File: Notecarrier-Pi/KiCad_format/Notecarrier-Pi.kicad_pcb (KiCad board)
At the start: 4 copper layers, 0 parts

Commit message: Port fab, silk and copper layers for Notecarrier-Pi.
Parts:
- added C1: 22u/25V-X5R, blues-kicad-lib:CS-C-1206, B.Cu at (71.8, 94.7)
- added C2: 22u/25V-X5R, blues-kicad-lib:CS-C-1206, B.Cu at (72.8, 102.9)
- added C3: 100n/16V, blues-kicad-lib:CS-C-0402, B.Cu at (97.6, 120.1)
- added C4: 33p/50V-C0G, blues-kicad-lib:CS-C-0402, B.Cu at (97.5, 122.6)
- added C5: 33p/50V-C0G, blues-kicad-lib:CS-C-0402, B.Cu at (103.4, 121.1)
- added C6: 33p/50V-C0G, blues-kicad-lib:CS-C-0402, B.Cu at (100.5, 123.0)
- added C7: 100n/16V, blues-kicad-lib:CS-C-0402, B.Cu at (75.2, 130.0)
- added C8: 10n/1kV, blues-kicad-lib:CS-C-1206, B.Cu at (72.8, 134.4)
- added DS1: STPS3H100U, blues-kicad-lib:SMB, B.Cu at (80.3, 109.4)
- added DS2: STPS3H100U, blues-kicad-lib:SMB, B.Cu at (80.3, 104.3)
- added DSW1: DIP-SW-CHS-01TB, blues-kicad-lib:DSS-CHS-01TB, B.Cu at (106.2, 96.6)
- added DSW2: DIP-SW-CHS-01TB, blues-kicad-lib:DSS-CHS-01TB, B.Cu at (114.1, 96.6)
- added DSW3: DIP-SW-CHS-01TB, blues-kicad-lib:DSS-CHS-01TB, B.Cu at (122.0, 96.6)
- added F1: SF-0603F150-2, blues-kicad-lib:FS-0603, B.Cu at (75.8, 94.6)
- added F2: 3.5A/32V, blues-kicad-lib:FS-0603, B.Cu at (96.7, 104.9)
- added FID1: TPS, blues-kicad-lib:FIDUCIAL, B.Cu at (67.0, 134.1)
- added FID2: TPS, blues-kicad-lib:FIDUCIAL, B.Cu at (127.6, 91.8)
- added FID3: TPS, blues-kicad-lib:FIDUCIAL, F.Cu at (127.6, 91.9)
- added FID4: TPS, blues-kicad-lib:FIDUCIAL, F.Cu at (67.4, 132.2)
- added H1: MountingHole, blues-kicad-lib:FORO-0270-U, F.Cu at (68.5, 87.5)
- added H2: MountingHole, blues-kicad-lib:FORO-0270-U, F.Cu at (126.5, 87.5)
- added H3: MountingHole, blues-kicad-lib:FORO-0270-U, F.Cu at (126.5, 136.5)
- added H4: MountingHole, blues-kicad-lib:FORO-0270-U, F.Cu at (68.5, 136.5)
- added J1: 2223, blues-kicad-lib:J-20x2-0254-FDT-SSQX03, B.Cu at (97.5, 87.5)
- added J2: NanoSIM - SF72S006VBAR2500, blues-kicad-lib:J-NANOSIM-SF72S006VBA_NO-FILL, B.Cu at (100.4, 132.4)
- added J3: MDT420E01001, blues-kicad-lib:J-75-0050-MOS-M2-E, F.Cu at (89.0, 97.8)
- added J4: 10118192-0002LF, blues-kicad-lib:J-5-0065-FOS-MICROUSB10118192, B.Cu at (69.7, 127.8)
- added J5: GROVE, blues-kicad-lib:J-4-0200-MOS-GROVE_NO-SILK, F.Cu at (118.8, 125.0)
- added OBJ1: 9774025151R, blues-kicad-lib:DIST-WASMSIM0250, F.Cu at (89.0, 131.0)
- added R1: 22R, blues-kicad-lib:RS-0603, B.Cu at (100.2, 120.6)
- added R10: 100R, blues-kicad-lib:RS-0402, B.Cu at (93.7, 93.2)
- added R11: 100R, blues-kicad-lib:RS-0402, B.Cu at (93.7, 95.2)
- added R12: 100R, blues-kicad-lib:RS-0402, B.Cu at (94.9, 93.2)
- added R13: 100R, blues-kicad-lib:RS-0402, B.Cu at (94.9, 95.2)
- added R2: 22R, blues-kicad-lib:RS-0603, B.Cu at (96.1, 120.6)
- added R3: 22R, blues-kicad-lib:RS-0603, B.Cu at (102.0, 120.6)
- added R4: 15k, blues-kicad-lib:RS-0402, B.Cu at (98.8, 120.1)
- added R5: 1M, blues-kicad-lib:RS-1206, B.Cu at (75.1, 134.4)
- added R6: 100R, blues-kicad-lib:RS-0402, B.Cu at (89.4, 93.2)
- added R7: 100R, blues-kicad-lib:RS-0402, B.Cu at (89.4, 95.2)
- added R8: 100R, blues-kicad-lib:RS-0402, B.Cu at (90.6, 93.2)
- added R9: 100R, blues-kicad-lib:RS-0402, B.Cu at (90.6, 95.2)
- added TVS1: SM6T6V8A, blues-kicad-lib:SMB, B.Cu at (80.6, 113.4)
- added TVS2: SM2T3V3A, blues-kicad-lib:D-DO216AA_NO-SILK, B.Cu at (70.7, 92.1)
- added TVS3: SM6T6V8A, blues-kicad-lib:SMB, B.Cu at (68.6, 98.3)
- added TVS4: ESDLC5V0M5-TP, blues-kicad-lib:SOT563, B.Cu at (106.6, 120.9)
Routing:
- net (no net): track 0.00 -> 230.5 mm
- net GND: track 0.00 -> 82.6 mm
- net /SIM_VCC: track 0.00 -> 64.2 mm
- net /SIM_NPRESENT: track 0.00 -> 48.6 mm
- net /USB_DM: track 0.00 -> 44.5 mm
- net /USB_DP: track 0.00 -> 43.8 mm
- net /SDA: track 0.00 -> 32.7 mm
- net /SIM_CLK: track 0.00 -> 32.2 mm
- net /SIM_IO: track 0.00 -> 31.7 mm
- net Net-(J3-VACT_GPS_IN): track 0.00 -> 29.8 mm
- net /SCL: track 0.00 -> 28.9 mm
- net /AUX_EN: track 0.00 -> 28.4 mm
- net VACT_GPS_OUT: track 0.00 -> 27.7 mm
- net /SIM_RST: track 0.00 -> 26.7 mm
- net VUSB: track 0.00 -> 24.8 mm
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- added copper zone on B.Cu, net GND
- added copper zone on In1.Cu, net GND
- added copper zone on In2.Cu, net GND
- added copper zone on B.Cu, net Net-(J4-Shield)
- added copper zone on B.Cu, net V+
- added copper zone on B.Cu, net VIO
- added copper zone on F.Cu, net VIO_P
- added copper zone on B.Cu, net VMODEM
- added copper zone on B.Cu, net VMODEM_P
- added copper zone on F.Cu, net VMODEM_P
- added copper zone on B.Cu, net VUSB
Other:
- board outline added: 65 x 56.5 mm
- board text added: "1 . 1"
- board text added: "1.1"
- board text added: "20173047_V4"
- board text added: "ACTIVE"
- board text added: "DS1"
- board text added: "DSW1"
- board text added: "DSW2"
- board text added: "DSW3"
- board text added: "J1"
- board text added: "NOTECARRIER-PI"
- board text added: "OFF"
- board text added: "ON"
- board text added: "R11"
- board text added: "R13"
- board text added: "R2"
- board text added: "R3"
- board text added: "R7"
- board text added: "SERIAL"
- board text added: "TVS3"
- board text added: "TVS4"
- board text added: "TXRX"
- board text removed: "1V8"
- board text removed: "2.0"
- board text removed: "2017-3047_V16"
- board text removed: "3V3"
- board text removed: "<BAT"
- board text removed: "<MAIN"
- board text removed: "<VIO"
- board text removed: "<VUSB"
- board text removed: "ANT1"
- board text removed: "ANT2"
- board text removed: "AUX1"
- board text removed: "AUX2"
- board text removed: "AUX3"
- board text removed: "AUX4"
- board text removed: "AUXEN"
- board text removed: "AUXRX"
- board text removed: "AUXTX"
- board text removed: "BAT1"
- board text removed: "C10"
- board text removed: "C11"
- board text removed: "C12"
- board text removed: "C13"
- board text removed: "C16"
- board text removed: "C17"
- board text removed: "C18"
- board text removed: "C19"
- board text removed: "C21"
- board text removed: "C22"
- board text removed: "C23"
- board text removed: "C25"
- board text removed: "C26"
- board text removed: "C27"
- board text removed: "C28"
- board text removed: "C29"
- board text removed: "C9"
- board text removed: "DS3"
- board text removed: "DS4"
- board text removed: "DS5"
- board text removed: "DS6"
- board text removed: "EN"
- board text removed: "GND"
- board text removed: "J10"
- board text removed: "J11"
- board text removed: "J12"
- board text removed: "J13"
- board text removed: "J14"
- board text removed: "J6"
- board text removed: "J7"
- board text removed: "J8"
- board text removed: "J9"
- board text removed: "L1"
- board text removed: "L2"
- board text removed: "L5"
- board text removed: "L6"
- board text removed: "L7"
- board text removed: "L8"
- board text removed: "L9"
- board text removed: "LIPO"
- board text removed: "MAIN"
- board text removed: "NN"
- board text removed: "NOTECARRIER-A"
- board text removed: "PAD1"
- board text removed: "PAD2"
- board text removed: "Port"
- board text removed: "Q1"
- board text removed: "QWIIC"
- board text removed: "R14"
- board text removed: "R15"
- board text removed: "R16"
- board text removed: "R18"
- board text removed: "R21"
- board text removed: "R22"
- board text removed: "R25"
- board text removed: "R26"
- board text removed: "R27"
- board text removed: "R28"
- board text removed: "R29"
- board text removed: "R30"
- board text removed: "R31"
- board text removed: "RR1"
- board text removed: "RR2"
- board text removed: "RST"
- board text removed: "RX"
- board text removed: "SOLAR"
- board text removed: "SW1"
- board text removed: "TX"
- board text removed: "U1"
- board text removed: "U2"
- board text removed: "U3"
- board text removed: "U5"
- board text removed: "USB Charging"
- board text removed: "V+"

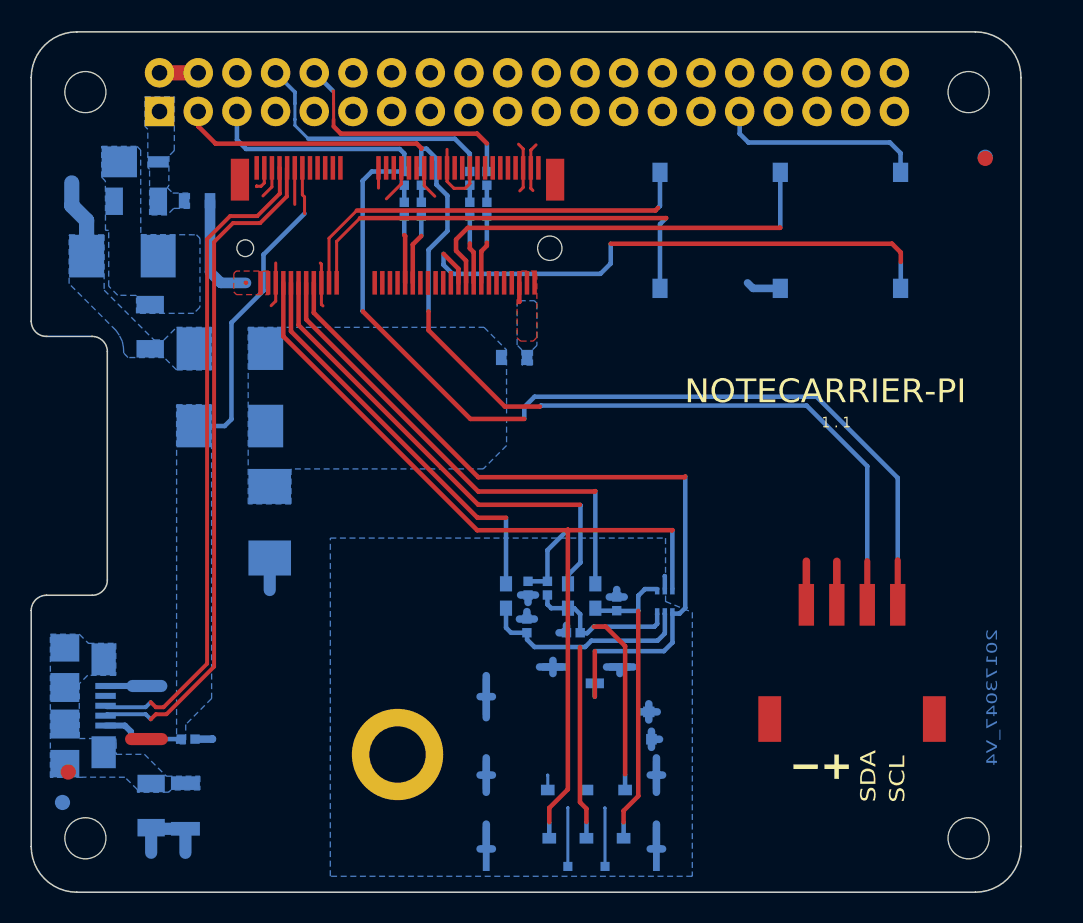
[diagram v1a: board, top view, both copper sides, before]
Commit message: Create rules and clearances to suit Notecarrier-Pi port.
Also, fix VIO_P power symbol which had VIO net name.
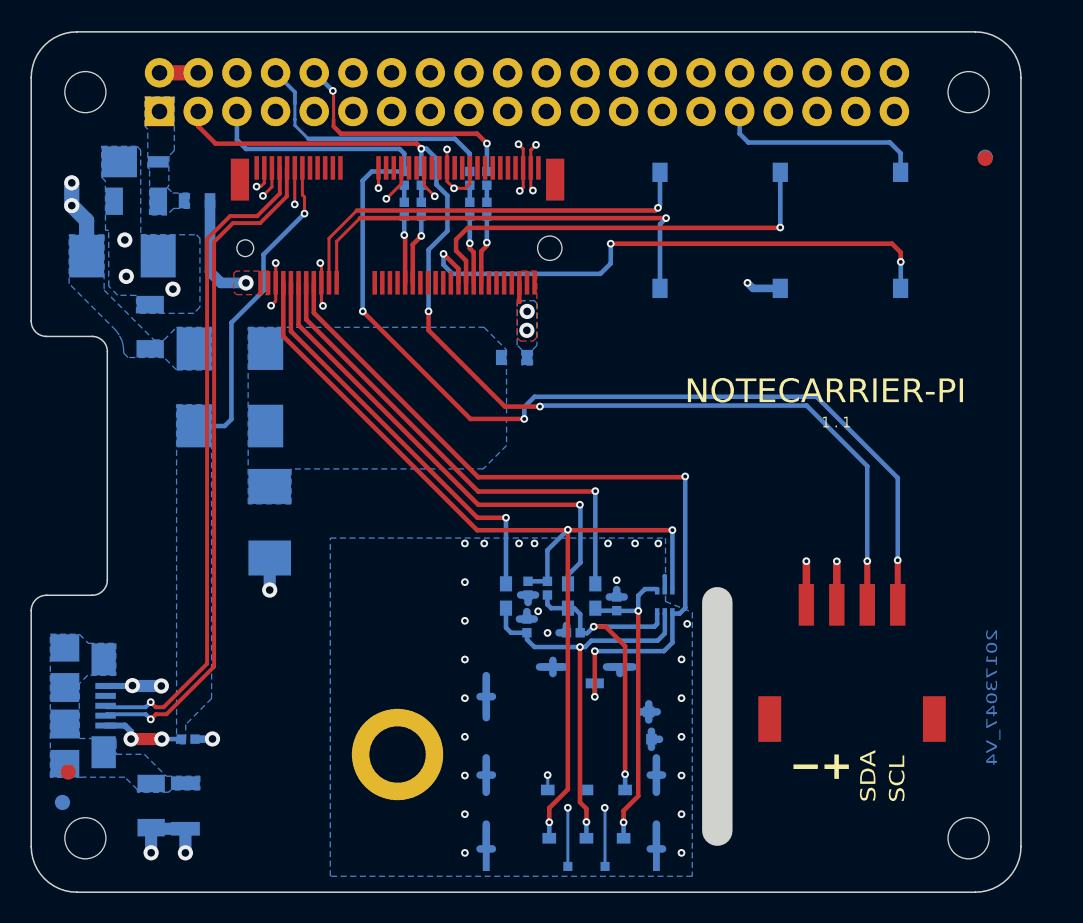
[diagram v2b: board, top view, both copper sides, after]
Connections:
- DSW2 pad 1: VIO -> VIO_P
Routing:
- net (no net): track 230.5 -> 0.00 mm
- net VIO_P: track 10.2 -> 67.9 mm, vias 0 -> 3
- net /SCL: track 28.9 -> 75.6 mm, vias 0 -> 3
- net /SDA: track 32.7 -> 72.8 mm, vias 0 -> 4
- net Net-(J3-ATTN_P): track 4.05 -> 37.5 mm, vias 0 -> 3
- net Net-(J2-CLK): track 6.36 -> 20.6 mm, vias 0 -> 2
- net /AUX_TX: track 3.56 -> 16.4 mm, vias 0 -> 2
- net Net-(J2-RST): track 15.2 -> 26.9 mm, vias 0 -> 2
- net Net-(J2-I/O): track 11.3 -> 22.3 mm, vias 0 -> 2
- net /SIM_NPRESENT: track 48.6 -> 51.6 mm, vias 0 -> 3
- net VIO: track 2.30 -> 0.00 mm
- net VUSB: track 24.8 -> 26.8 mm, vias 0 -> 3
- net VMODEM_P: vias 0 -> 2
- net VACT_GPS_OUT: vias 0 -> 1
- net V+: vias 0 -> 2
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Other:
- outline, holes or cut-outs redrawn

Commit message: Complete validation of Notecarrier-Pi port.
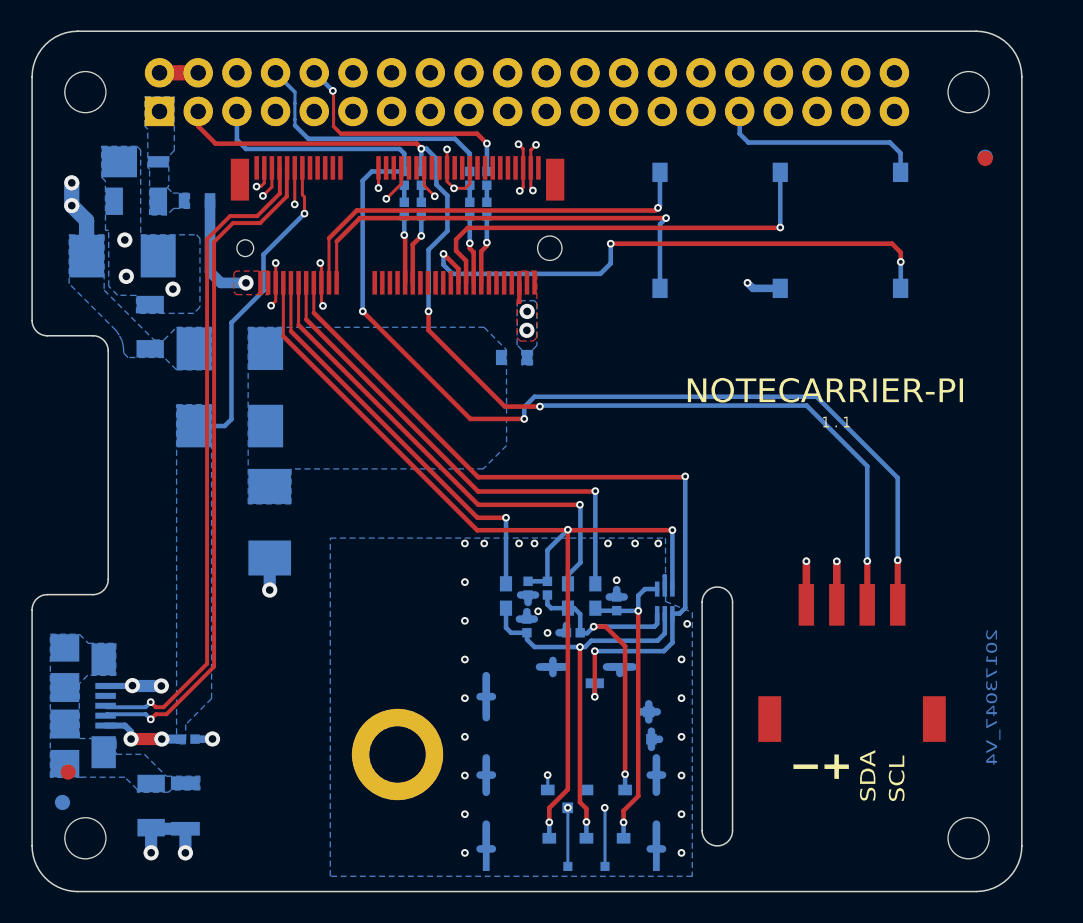
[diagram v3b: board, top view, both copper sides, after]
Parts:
- H1, H2, H3, H4: footprint blues-kicad-lib:FORO-0270-U -> blues-kicad-lib:FORO-0270-U_smaller-clearance
- J4: footprint blues-kicad-lib:J-5-0065-FOS-MICROUSB10118192 -> blues-kicad-lib:J-5-0065-FOS-USB10118192-NOF
- TVS4: footprint blues-kicad-lib:SOT563 -> blues-kicad-lib:SOT666_NO-SILK
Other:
- outline, holes or cut-outs redrawn
- board text added: "+/- 10%"
- board text added: "0 mm"
- board text added: "0.02 mm"
- board text added: "0.035 mm"
- board text added: "0.2"
- board text added: "0.2 mm"
- board text added: "0.2000 mm / 0.2000 mm"
- board text added: "0.2540 mm"
- board text added: "0.26"
- board text added: "1 mm"
- board text added: "1.5800 mm"
- board text added: "4"
- board text added: "65.0000 mm x 56.5000 mm"
- board text added: "90 ohm"
- board text added: "B.Cu"
- board text added: "B.Mask"
- board text added: "B.Paste"
- board text added: "B.Silkscreen"
- board text added: "BOARD CHARACTERISTICS"
- board text added: "Board Thickness:"
- board text added: "Board overall dimensions:"
- board text added: "Bottom Silk Screen"
- board text added: "Bottom Solder Mask"
- board text added: "Bottom Solder Paste"
- board text added: "Castellated pads:"
- board text added: "Color"
- board text added: "Copper Finish:"
- board text added: "Copper Layer Count:"
- board text added: "Dielectric 1"
- board text added: "Dielectric 2"
- board text added: "Dielectric 3"
- board text added: "ENIG"
- board text added: "Edge card connectors:"
- board text added: "F.Cu"
- board text added: "F.Cu and B.Cu thickness layer shown in the table above contains +20um (from IPC-A-600 Class 2) of plating"
- board text added: "F.Mask"
- board text added: "F.Paste"
- board text added: "F.Silkscreen"
- board text added: "FR4-TG150"
- board text added: "Green"
- board text added: "IMPEDANCE CONTROL TABLE"
- board text added: "IMPEDANCE DIFFERENTIAL"
- board text added: "IMPEDANCE SINGLE-ENDED"
- board text added: "Impedance Control:"
- board text added: "In1.Cu"
- board text added: "In2.Cu"
- board text added: "LAYER"
- board text added: "Layer Name"
- board text added: "Material"
- board text added: "Min hole diameter:"
- board text added: "Min track/spacing:"
- board text added: "NA"
- board text added: "No"
- board text added: "Not specified"
- board text added: "PUT PCB DATA/LOGO/CODE IN THIS AREA ON BOTTOM LAYER"
- board text added: "Plated Board Edge:"
- board text added: "SPACING [MM]"
- board text added: "TOLLERANCE"
- board text added: "TRACE [MM]"
- board text added: "Thickness (mm)"
- board text added: "Top Silk Screen"
- board text added: "Top Solder Mask"
- board text added: "Top Solder Paste"
- board text added: "Type"
- board text added: "White"
- board text added: "Yes"
- board text added: "copper"
- board text added: "core"
- board text added: "prepreg"
- board text removed: "1"
- board text removed: "1.1"
- board text removed: "C1"
- board text removed: "C2"
- board text removed: "C3"
- board text removed: "C4"
- board text removed: "C5"
- board text removed: "C6"
- board text removed: "C7"
- board text removed: "C8"
- board text removed: "DS1"
- board text removed: "DS2"
- board text removed: "DSW1"
- board text removed: "DSW2"
- board text removed: "DSW3"
- board text removed: "EDGE"
- board text removed: "F1"
- board text removed: "F2"
- board text removed: "FID1"
- board text removed: "FID2"
- board text removed: "FID3"
- board text removed: "FID4"
- board text removed: "J1"
- board text removed: "J2"
- board text removed: "J3"
- board text removed: "J4"
- board text removed: "J5"
- board text removed: "OBJ1"
- board text removed: "Only GND Trace"
- board text removed: "R1"
- board text removed: "R10"
- board text removed: "R11"
- board text removed: "R12"
- board text removed: "R13"
- board text removed: "R2"
- board text removed: "R3"
- board text removed: "R4"
- board text removed: "R5"
- board text removed: "R6"
- board text removed: "R7"
- board text removed: "R8"
- board text removed: "R9"
- board text removed: "TVS1"
- board text removed: "TVS2"
- board text removed: "TVS3"
- board text removed: "TVS4"
